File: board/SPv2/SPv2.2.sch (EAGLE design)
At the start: 35 parts, among them IC1 S34ML0XG1, IC2 F5508, IC4 74LS14D, Q1 12MHz

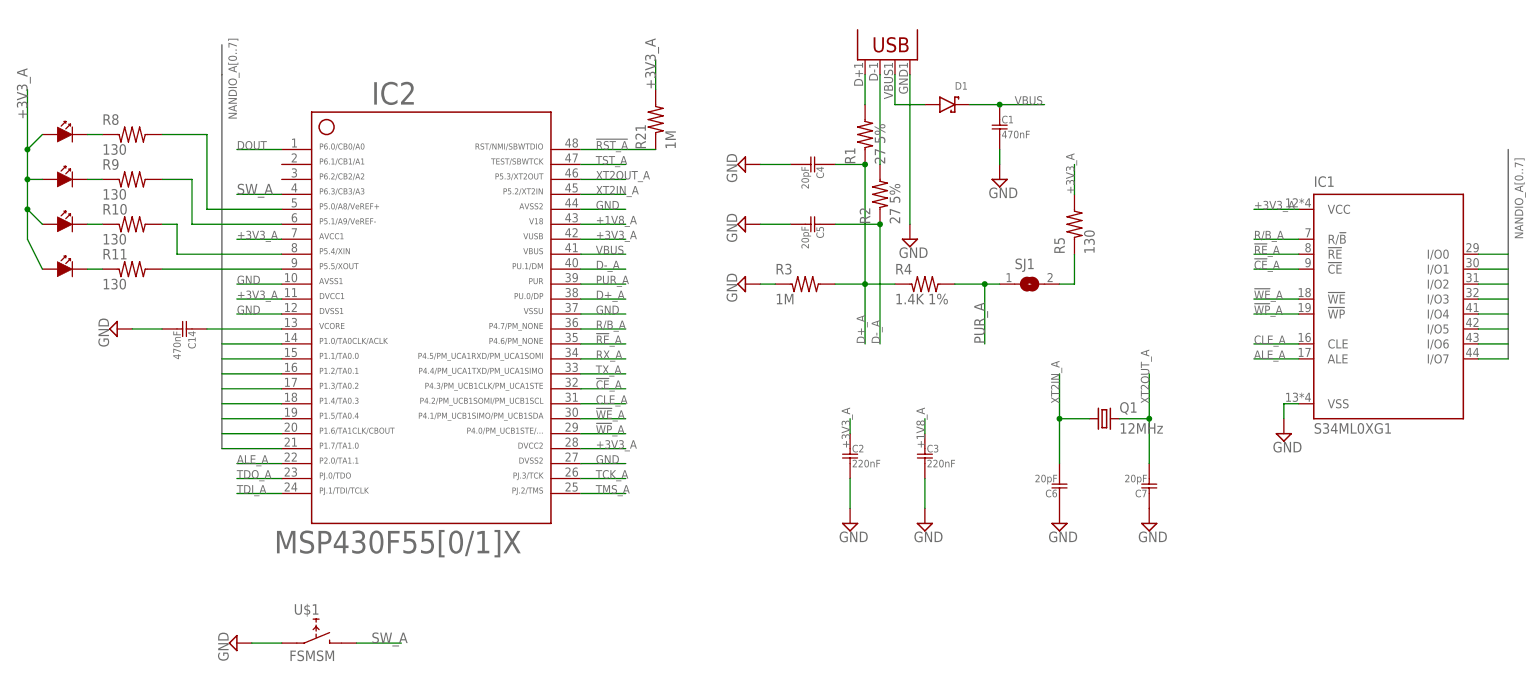
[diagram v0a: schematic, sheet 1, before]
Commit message: new switch smaller 74ls14 jumper header instead of solder jumper board layout in progress
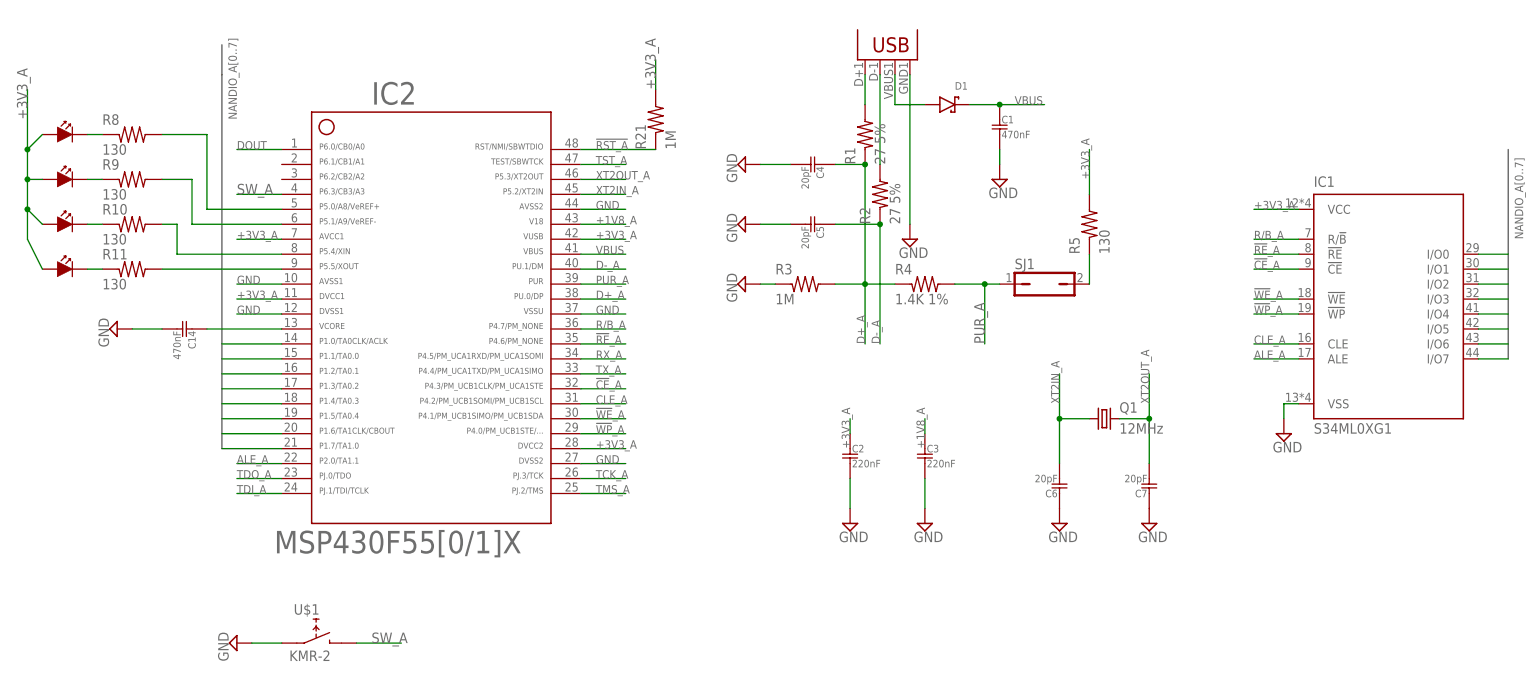
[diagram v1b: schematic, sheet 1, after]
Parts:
- IC4: value 74LS14D -> 74LS14DB; device 74xx-us:74LS14D -> 74xx-db-us:74LS14DB
- SJ1: device jumper:SJW -> jumper:JP1Q
- U$1: value FSMSM -> KMR-2; device Passives:FSMSM -> Passives:KMR-2
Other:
- moved on the sheet: R5
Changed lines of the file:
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@@
 <layer number="54" name="bGND_GNDA" color="1" fill="9" visible="no" active="no"/>
 <layer number="56" name="wert" color="7" fill="1" visible="no" active="no"/>
+<layer number="90" name="Modules" color="5" fill="1" visible="yes" active="yes"/>
 <layer number="91" name="Nets" color="2" fill="1" visible="yes" active="yes"/>
 <layer number="92" name="Busses" color="1" fill="1" visible="yes" active="yes"/>
@@
 <part name="R2" library="Passives" deviceset="R" device="0805" value="27 5%"/>
 <part name="Q1" library="Passives" deviceset="CRYSTAL" device="CSM-3X" value="12MHz"/>
-<part name="U$1" library="Passives" deviceset="FSMSM" device=""/>
+<part name="U$1" library="Passives" deviceset="KMR-2" device=""/>
 <part name="R3" library="Passives" deviceset="R" device="0805" value="1M"/>
 <part name="SUPPLY10" library="supply2" deviceset="GND" device=""/>
@@
 <part name="R11" library="Passives" deviceset="R" device="0805" value="130"/>
 <part name="D1" library="Passives" deviceset="D-SCHOTTKY" device=""/>
-<part name="IC4" library="74xx-us" deviceset="74*14" device="D" technology="LS"/>
+<part name="IC4" library="74xx-db-us" deviceset="74*14" device="DB" technology="LS"/>
 <part name="SUPPLY12" library="supply2" deviceset="GND" device=""/>
 <part name="R6" library="Passives" deviceset="R" device="0805" value="1.4k"/>
 <part name="R7" library="Passives" deviceset="R" device="0805" value="1.4k"/>
 <part name="SUPPLY13" library="supply2" deviceset="GND" device=""/>
-<part name="SJ1" library="jumper" deviceset="SJ" device="W"/>
+<part name="SJ1" library="jumper" deviceset="JP1Q" device=""/>
 <part name="SUPPLY14" library="supply2" deviceset="GND" device=""/>
 <part name="U$2" library="Passives" deviceset="SNAP-HALF" device=""/>
@@
 <instance part="SUPPLY10" gate="GND" x="101.6" y="93.98" rot="R270"/>
 <instance part="R4" gate="G$1" x="132.08" y="93.98"/>
-<instance part="R5" gate="G$1" x="157.48" y="104.14" rot="R90"/>
+<instance part="R5" gate="G$1" x="160.02" y="104.14" rot="R90"/>
 <instance part="C14" gate="G$1" x="5.08" y="86.36" rot="R270"/>
 <instance part="SUPPLY18" gate="GND" x="-5.08" y="86.36" rot="R270"/>
@@
 <instance part="R11" gate="G$1" x="-2.54" y="96.52"/>
 <instance part="D1" gate="G$1" x="137.16" y="124.46"/>
-<instance part="SJ1" gate="1" x="149.86" y="93.98"/>
+<instance part="SJ1" gate="A" x="152.4" y="93.98" rot="R270"/>
 <instance part="SUPPLY14" gate="GND" x="15.24" y="33.02" rot="R270"/>
 </instances>
@@
 <segment>
 <pinref part="R5" gate="G$1" pin="2"/>
-<wire x1="157.48" y1="109.22" x2="157.48" y2="114.3" width="0.1524" layer="91"/>
-<label x="157.48" y="109.22" size="1.4224" layer="95" rot="R90"/>
+<wire x1="160.02" y1="109.22" x2="160.02" y2="116.84" width="0.1524" layer="91"/>
+<label x="160.02" y="111.76" size="1.4224" layer="95" rot="R90"/>
 </segment>
 <segment>
@@
 </segment>
 <segment>
-<pinref part="SJ1" gate="1" pin="1"/>
+<pinref part="SJ1" gate="A" pin="1"/>
 <pinref part="R4" gate="G$1" pin="2"/>
 <wire x1="144.78" y1="93.98" x2="142.24" y2="93.98" width="0.1524" layer="91"/>
@@
 <segment>
 <pinref part="R5" gate="G$1" pin="1"/>
-<wire x1="157.48" y1="99.06" x2="157.48" y2="93.98" width="0.1524" layer="91"/>
-<pinref part="SJ1" gate="1" pin="2"/>
-<wire x1="157.48" y1="93.98" x2="154.94" y2="93.98" width="0.1524" layer="91"/>
-</segment>
-</net>
+<wire x1="160.02" y1="99.06" x2="160.02" y2="93.98" width="0.1524" layer="91"/>
+<pinref part="SJ1" gate="A" pin="2"/>
+</segment>
+</net>

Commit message: rerouting in progress
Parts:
- added TP1, TP2, TP3, TP4: TPTP13R, testpad:TPTP13R
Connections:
- net GND: now also TP4.TP
- net N$1: now also TP1.TP
- net N$2: now also TP2.TP
- net N$33: now also TP3.TP
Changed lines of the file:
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@@
 <part name="U$3" library="Passives" deviceset="FIDUCAL" device=""/>
 <part name="U$12" library="Passives" deviceset="FIDUCAL" device=""/>
+<part name="TP1" library="testpad" deviceset="TP" device="TP13R"/>
+<part name="TP2" library="testpad" deviceset="TP" device="TP13R"/>
+<part name="TP3" library="testpad" deviceset="TP" device="TP13R"/>
+<part name="TP4" library="testpad" deviceset="TP" device="TP13R"/>
 </parts>
 <sheets>
@@
 <instance part="SJ1" gate="A" x="152.4" y="93.98" rot="R270"/>
 <instance part="SUPPLY14" gate="GND" x="15.24" y="33.02" rot="R270"/>
+<instance part="TP1" gate="G$1" x="109.22" y="127" rot="R90"/>
+<instance part="TP2" gate="G$1" x="104.14" y="124.46" rot="R90"/>
+<instance part="TP3" gate="G$1" x="132.08" y="134.62"/>
+<instance part="TP4" gate="G$1" x="134.62" y="114.3" rot="R270"/>
 </instances>
 <busses>
@@
 <pinref part="JP1" gate="G$1" pin="GND"/>
 <pinref part="SUPPLY5" gate="GND" pin="GND"/>
-<wire x1="129.54" y1="129.54" x2="129.54" y2="104.14" width="0.1524" layer="91"/>
+<wire x1="129.54" y1="129.54" x2="129.54" y2="114.3" width="0.1524" layer="91"/>
+<pinref part="TP4" gate="G$1" pin="TP"/>
+<wire x1="129.54" y1="114.3" x2="129.54" y2="104.14" width="0.1524" layer="91"/>
+<wire x1="132.08" y1="114.3" x2="129.54" y2="114.3" width="0.1524" layer="91"/>
+<junction x="129.54" y="114.3"/>
 </segment>
 </net>
@@
 <pinref part="JP1" gate="G$1" pin="D+"/>
 <pinref part="R1" gate="G$1" pin="2"/>
-<wire x1="121.92" y1="124.46" x2="121.92" y2="129.54" width="0.1524" layer="91"/>
+<wire x1="121.92" y1="124.46" x2="121.92" y2="127" width="0.1524" layer="91"/>
+<pinref part="TP1" gate="G$1" pin="TP"/>
+<wire x1="121.92" y1="127" x2="121.92" y2="129.54" width="0.1524" layer="91"/>
+<wire x1="111.76" y1="127" x2="121.92" y2="127" width="0.1524" layer="91"/>
+<junction x="121.92" y="127"/>
 </segment>
 </net>
@@
 <pinref part="JP1" gate="G$1" pin="D-"/>
 <pinref part="R2" gate="G$1" pin="2"/>
-<wire x1="124.46" y1="114.3" x2="124.46" y2="129.54" width="0.1524" layer="91"/>
+<wire x1="124.46" y1="114.3" x2="124.46" y2="124.46" width="0.1524" layer="91"/>
+<pinref part="TP2" gate="G$1" pin="TP"/>
+<wire x1="124.46" y1="124.46" x2="124.46" y2="129.54" width="0.1524" layer="91"/>
+<wire x1="106.68" y1="124.46" x2="124.46" y2="124.46" width="0.1524" layer="91"/>
+<junction x="124.46" y="124.46"/>
 </segment>
 </net>
@@
 <wire x1="132.08" y1="124.46" x2="127" y2="124.46" width="0.1524" layer="91"/>
 <wire x1="127" y1="124.46" x2="127" y2="129.54" width="0.1524" layer="91"/>
-</segment>
-</net>
+<pinref part="TP3" gate="G$1" pin="TP"/>
+<wire x1="132.08" y1="132.08" x2="132.08" y2="124.46" width="0.1524" layer="91"/>
+<junction x="132.08" y="124.46"/>
+</segment>
+</net>

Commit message: finished v2.2, twinned board for fab
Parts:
- removed U$12: FIDUCAL, Passives:FIDUCAL
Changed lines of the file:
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@@
 <part name="U$2" library="Passives" deviceset="SNAP-HALF" device=""/>
 <part name="U$3" library="Passives" deviceset="FIDUCAL" device=""/>
-<part name="U$12" library="Passives" deviceset="FIDUCAL" device=""/>
 <part name="TP1" library="testpad" deviceset="TP" device="TP13R"/>
 <part name="TP2" library="testpad" deviceset="TP" device="TP13R"/>
@@
 <instance part="U$2" gate="G$1" x="-35.56" y="38.1"/>
 <instance part="U$3" gate="G$1" x="-7.62" y="60.96"/>
-<instance part="U$12" gate="G$1" x="5.08" y="60.96"/>
 </instances>
 <busses>

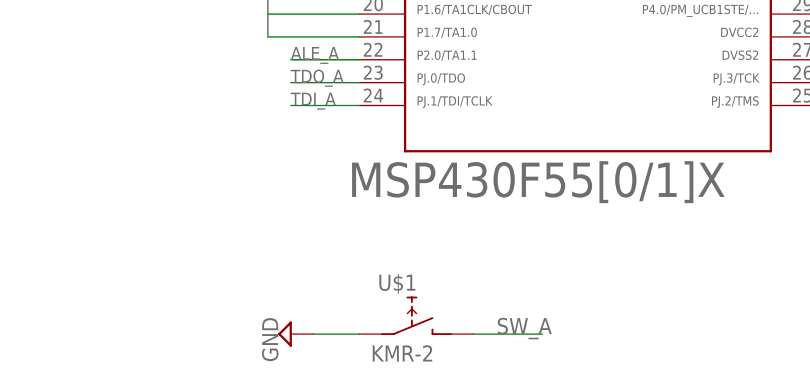
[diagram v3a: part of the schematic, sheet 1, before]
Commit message: finalizing half-board, switch testing remains
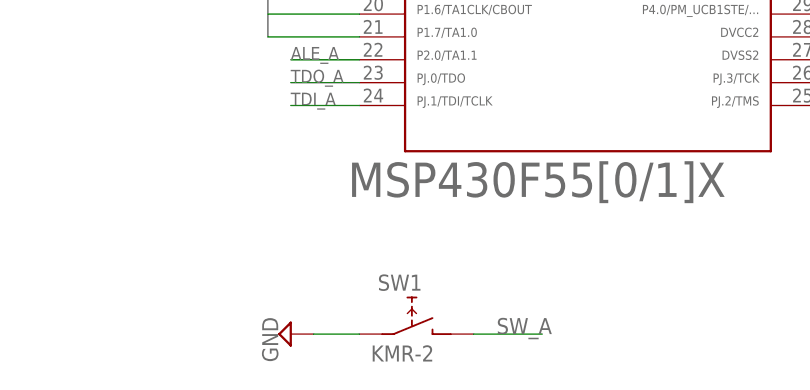
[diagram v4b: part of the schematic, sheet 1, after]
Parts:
- renumbered U$1 to SW1
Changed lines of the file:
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@@
 <part name="R2" library="Passives" deviceset="R" device="0805" value="27 5%"/>
 <part name="Q1" library="Passives" deviceset="CRYSTAL" device="CSM-3X" value="12MHz"/>
-<part name="U$1" library="Passives" deviceset="KMR-2" device=""/>
+<part name="SW1" library="Passives" deviceset="KMR-2" device=""/>
 <part name="R3" library="Passives" deviceset="R" device="0805" value="1M"/>
 <part name="SUPPLY10" library="supply2" deviceset="GND" device=""/>
@@
 <instance part="R2" gate="G$1" x="124.46" y="109.22" rot="R90"/>
 <instance part="Q1" gate="G$1" x="162.56" y="71.12"/>
-<instance part="U$1" gate="G$1" x="27.94" y="35.56"/>
+<instance part="SW1" gate="G$1" x="27.94" y="35.56"/>
 <instance part="R3" gate="G$1" x="111.76" y="93.98"/>
 <instance part="SUPPLY10" gate="GND" x="101.6" y="93.98" rot="R270"/>
@@
 <segment>
 <pinref part="SUPPLY14" gate="GND" pin="GND"/>
-<pinref part="U$1" gate="G$1" pin="A1"/>
+<pinref part="SW1" gate="G$1" pin="A1"/>
 <wire x1="17.78" y1="33.02" x2="22.86" y2="33.02" width="0.1524" layer="91"/>
 </segment>
@@
 <net name="SW_A" class="0">
 <segment>
-<pinref part="U$1" gate="G$1" pin="B"/>
+<pinref part="SW1" gate="G$1" pin="B"/>
 <wire x1="35.56" y1="33.02" x2="43.18" y2="33.02" width="0.1524" layer="91"/>
 <label x="38.1" y="33.02" size="1.778" layer="95"/>
